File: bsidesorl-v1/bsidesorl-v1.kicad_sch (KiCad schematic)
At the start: 8 parts, among them J1 Conn_02x03_Top_Bottom, SW1 MST22D18G2 125

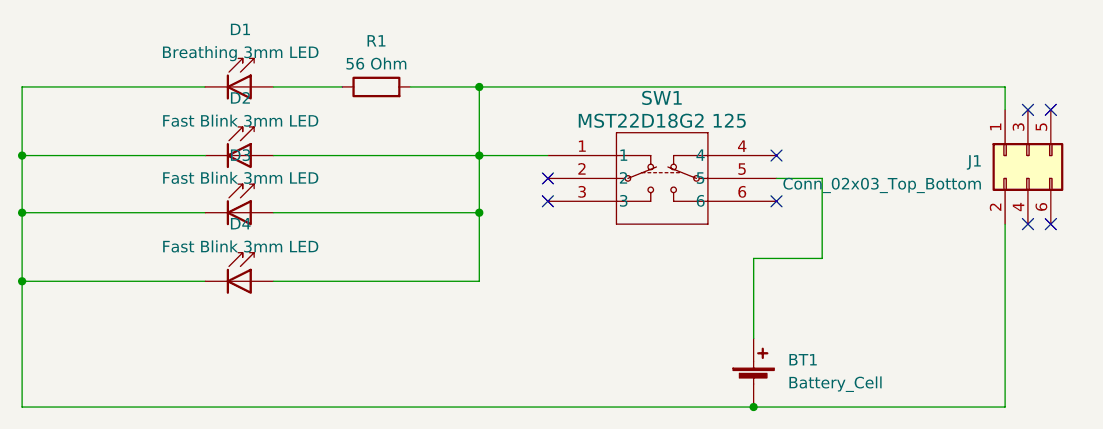
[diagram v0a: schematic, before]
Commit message: introduced additional sao
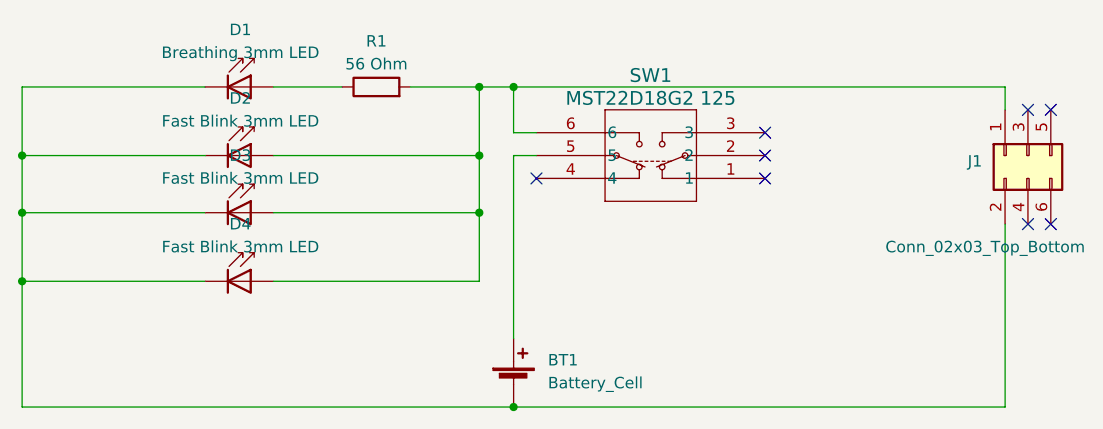
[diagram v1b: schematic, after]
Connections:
- net at D2.2 (A), D3.2 (A), D4.2 (A)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: now also SW1.6; no longer SW1.1
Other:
- moved on the sheet: BT1, SW1
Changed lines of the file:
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@@
   (junction (at 36.83 60.96) (diameter 0) (color 0 0 0 0)
-  )
-  (junction (at 118.11 74.93) (diameter 0) (color 0 0 0 0)
   )
   (junction (at 36.83 53.34) (diameter 0) (color 0 0 0 0)
@@
   (junction (at 36.83 46.99) (diameter 0) (color 0 0 0 0)
   )
-  (no_connect (at 120.65 46.99))
-  (no_connect (at 95.25 52.07))
+  (junction (at 91.44 39.37) (diameter 0) (color 0 0 0 0)
+  )
+  (junction (at 91.44 74.93) (diameter 0) (color 0 0 0 0)
+  )
+  (no_connect (at 119.38 44.45))
+  (no_connect (at 119.38 49.53))
   (no_connect (at 151.13 41.91))
-  (no_connect (at 95.25 49.53))
+  (no_connect (at 93.98 49.53))
   (no_connect (at 148.59 54.61))
-  (no_connect (at 120.65 52.07))
+  (no_connect (at 119.38 46.99))
   (no_connect (at 148.59 41.91))
   (no_connect (at 151.13 54.61))
-  (wire (pts (xy 118.11 67.31) (xy 118.11 58.42))
+  (wire (pts (xy 91.44 44.45) (xy 91.44 39.37))
+    (stroke (width 0) (type default))
+  )
+  (wire (pts (xy 91.44 46.99) (xy 91.44 67.31))
+    (stroke (width 0) (type default))
+  )
+  (wire (pts (xy 91.44 39.37) (xy 146.05 39.37))
     (stroke (width 0) (type default))
   )
@@
     (stroke (width 0) (type default))
   )
-  (wire (pts (xy 36.83 74.93) (xy 118.11 74.93))
+  (wire (pts (xy 87.63 39.37) (xy 87.63 46.99))
+    (stroke (width 0) (type default))
+  )
+  (wire (pts (xy 36.83 74.93) (xy 91.44 74.93))
     (stroke (width 0) (type default))
   )
@@
     (stroke (width 0) (type default))
   )
-  (wire (pts (xy 146.05 74.93) (xy 118.11 74.93))
+  (wire (pts (xy 91.44 74.93) (xy 146.05 74.93))
     (stroke (width 0) (type default))
   )
@@
     (stroke (width 0) (type default))
   )
-  (wire (pts (xy 87.63 39.37) (xy 87.63 46.99))
-    (stroke (width 0) (type default))
-  )
   (wire (pts (xy 36.83 46.99) (xy 57.15 46.99))
-    (stroke (width 0) (type default))
-  )
-  (wire (pts (xy 118.11 58.42) (xy 125.73 58.42))
     (stroke (width 0) (type default))
   )
@@
     (stroke (width 0) (type default))
   )
+  (wire (pts (xy 91.44 46.99) (xy 93.98 46.99))
+    (stroke (width 0) (type default))
+  )
+  (wire (pts (xy 91.44 44.45) (xy 93.98 44.45))
+    (stroke (width 0) (type default))
+  )
   (wire (pts (xy 146.05 39.37) (xy 146.05 41.91))
     (stroke (width 0) (type default))
   )
   (wire (pts (xy 87.63 46.99) (xy 87.63 53.34))
-    (stroke (width 0) (type default))
-  )
-  (wire (pts (xy 125.73 49.53) (xy 120.65 49.53))
-    (stroke (width 0) (type default))
-  )
-  (wire (pts (xy 87.63 46.99) (xy 95.25 46.99))
     (stroke (width 0) (type default))
   )
@@
     (stroke (width 0) (type default))
   )
-  (wire (pts (xy 146.05 39.37) (xy 87.63 39.37))
+  (wire (pts (xy 87.63 39.37) (xy 91.44 39.37))
     (stroke (width 0) (type default))
   )
@@
     (stroke (width 0) (type default))
   )
-  (wire (pts (xy 125.73 58.42) (xy 125.73 49.53))
-    (stroke (width 0) (type default))
-  )
-  (symbol (lib_id "power switch:MST22D18G2_125") (at 95.25 46.99 0) (unit 1)
+  (symbol (lib_id "power switch:MST22D18G2_125") (at 119.38 49.53 180) (unit 1)
     (in_bom yes) (on_board yes) (dnp no) (fields_autoplaced)
-    (property "Reference" "SW1" (at 107.95 40.64 0)
+    (property "Reference" "SW1" (at 106.68 38.1 0)
       (effects (font (size 1.524 1.524)))
     )
-    (property "Value" "MST22D18G2 125" (at 107.95 43.18 0)
+    (property "Value" "MST22D18G2 125" (at 106.68 40.64 0)
       (effects (font (size 1.524 1.524)))
     )
-    (property "Footprint" "Power Switch:SOIC6_SW6_MST22D18G2_SHN" (at 100.33 38.1 0)
+    (property "Footprint" "Power Switch:SOIC6_SW6_MST22D18G2_SHN" (at 114.3 58.42 0)
       (effects (font (size 1.27 1.27) italic) hide)
     )
-    (property "Datasheet" "MST22D18G2 125" (at 107.95 55.88 0)
+    (property "Datasheet" "MST22D18G2 125" (at 106.68 40.64 0)
       (effects (font (size 1.27 1.27) italic) hide)
     )
@@
       (effects (font (size 1.27 1.27)) (justify left))
     )
-    (property "Value" "Conn_02x03_Top_Bottom" (at 143.51 50.165 90)
+    (property "Value" "Conn_02x03_Top_Bottom" (at 154.94 57.15 90)
       (effects (font (size 1.27 1.27)) (justify left))
     )
@@
     )
   )
-  (symbol (lib_id "Device:Battery_Cell") (at 118.11 72.39 0) (unit 1)
+  (symbol (lib_id "Device:Battery_Cell") (at 91.44 72.39 0) (unit 1)
     (in_bom yes) (on_board yes) (dnp no) (fields_autoplaced)
-    (property "Reference" "BT1" (at 121.92 69.723 0)
+    (property "Reference" "BT1" (at 95.25 69.723 0)
       (effects (font (size 1.27 1.27)) (justify left))
     )
-    (property "Value" "Battery_Cell" (at 121.92 72.263 0)
+    (property "Value" "Battery_Cell" (at 95.25 72.263 0)
       (effects (font (size 1.27 1.27)) (justify left))
     )
-    (property "Footprint" "Battery:BatteryHolder_Keystone_3002_1x2032" (at 118.11 70.866 90)
+    (property "Footprint" "Battery:BatteryHolder_Keystone_3002_1x2032" (at 91.44 70.866 90)
       (effects (font (size 1.27 1.27)) hide)
     )
-    (property "Datasheet" "~" (at 118.11 70.866 90)
+    (property "Datasheet" "~" (at 91.44 70.866 90)
       (effects (font (size 1.27 1.27)) hide)
     )
